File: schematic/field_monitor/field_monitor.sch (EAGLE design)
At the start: 4 parts, among them Q1 MOSFET-NCHANNELFQP30N06L

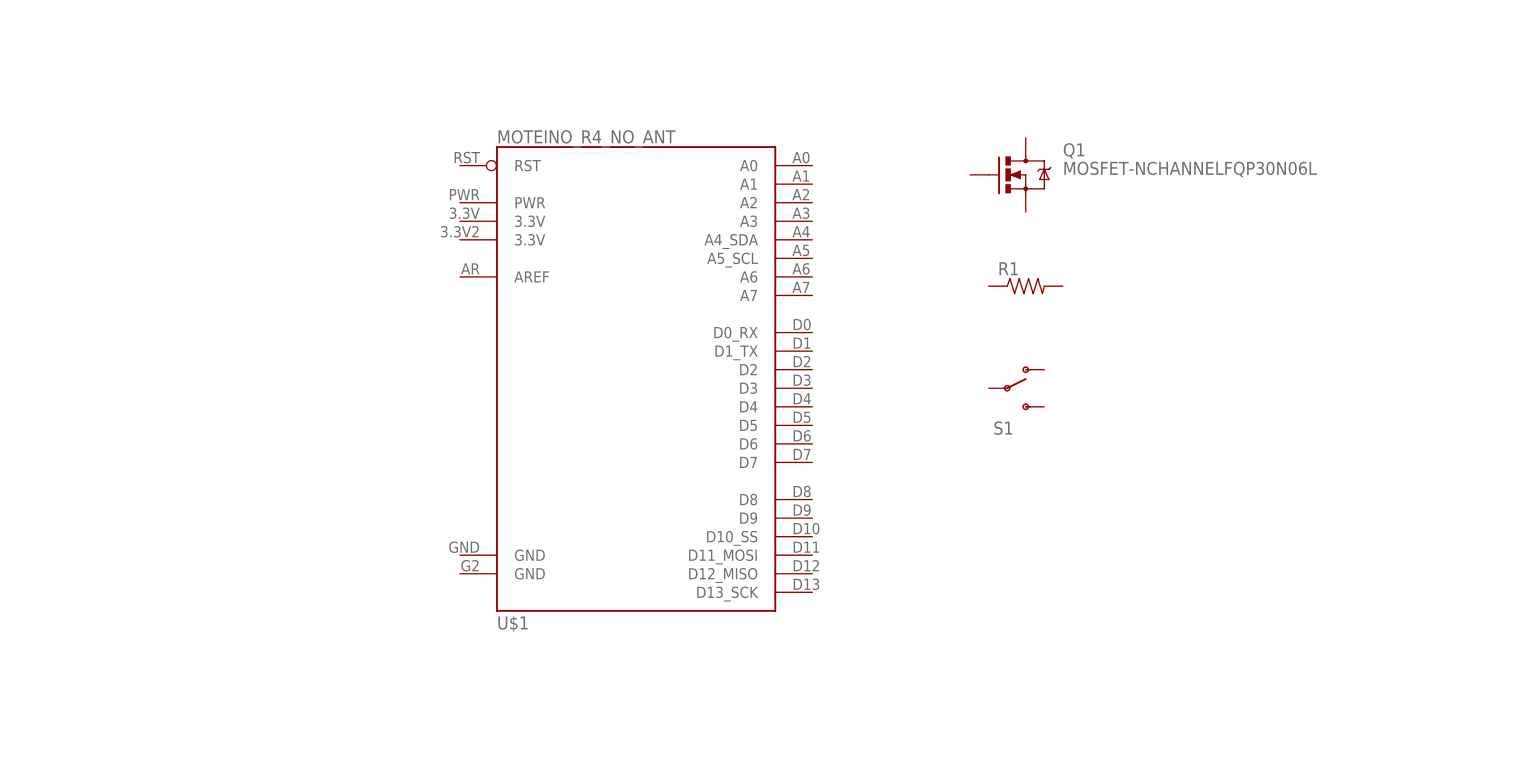
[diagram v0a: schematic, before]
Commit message: Adding basic components to schematic
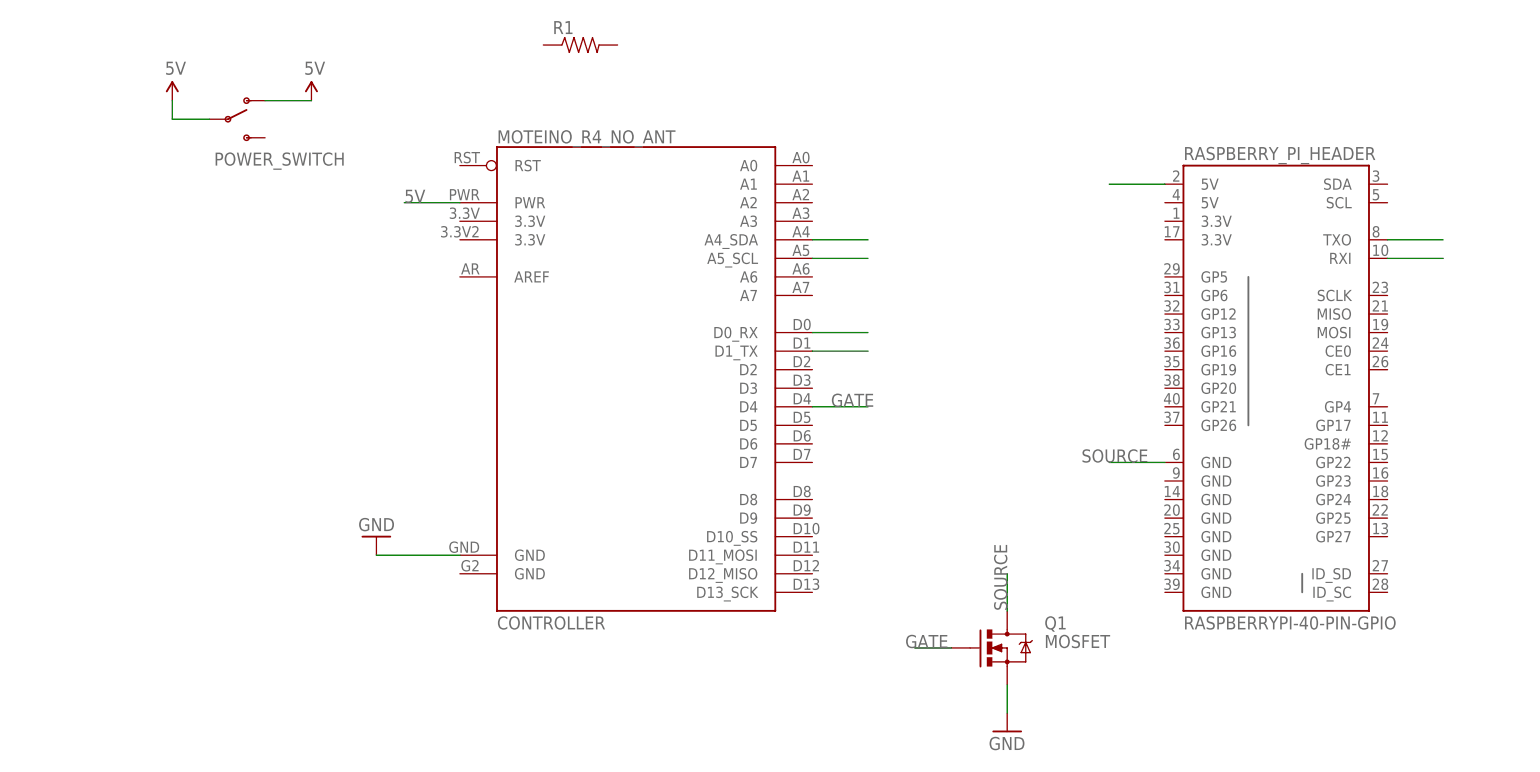
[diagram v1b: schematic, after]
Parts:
- removed S1: (no value), SparkFun-Electromechanical:SWITCH-SPDTPTH
- added POWER_SWITCH: (no value), SparkFun-Electromechanical:SWITCH-SPDTPTH
- added RASPBERRY_PI_HEADER: RASPBERRYPI-40-PIN-GPIO, SparkFun-Boards:RASPBERRYPI-40-PIN-GPIO
- Q1: value MOSFET-NCHANNELFQP30N06L -> MOSFET
- renumbered U$1 to CONTROLLER
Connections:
- new net 5V: CONTROLLER.PWR, POWER_SWITCH.O, POWER_SWITCH.P, RASPBERRY_PI_HEADER.5V@2
- new net GATE: CONTROLLER.D4, Q1.G
- new net GND: CONTROLLER.GND@1, Q1.S
- new net N$10: RASPBERRY_PI_HEADER.TXO
- new net N$11: RASPBERRY_PI_HEADER.RXI
- new net N$3: CONTROLLER.A5_SCL
- new net N$4: CONTROLLER.A4_SDA
- new net N$5: CONTROLLER.D0_RX
- new net N$6: CONTROLLER.D1_TX
- new net SOURCE: Q1.D, RASPBERRY_PI_HEADER.GND@6
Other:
- moved on the sheet: Q1, R1
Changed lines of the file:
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@@
 <layer number="112" name="tSilk" color="7" fill="1" visible="yes" active="yes"/>
 <layer number="113" name="IDFDebug" color="7" fill="1" visible="yes" active="yes"/>
+<layer number="114" name="Badge_Outline" color="11" fill="1" visible="no" active="no"/>
 <layer number="116" name="Patch_BOT" color="7" fill="1" visible="yes" active="yes"/>
 <layer number="118" name="Rect_Pads" color="7" fill="1" visible="yes" active="yes"/>
@@
 </classes>
 <parts>
-<part name="U$1" library="MoteinoR4Mod" deviceset="MOTEINO_R4_NO_ANT" device=""/>
-<part name="Q1" library="SparkFun-DiscreteSemi" deviceset="MOSFET-NCHANNEL" device="FQP30N06L"/>
+<part name="CONTROLLER" library="MoteinoR4Mod" deviceset="MOTEINO_R4_NO_ANT" device=""/>
+<part name="Q1" library="SparkFun-DiscreteSemi" deviceset="MOSFET-NCHANNEL" device="FQP30N06L" value="MOSFET"/>
 <part name="R1" library="SparkFun-Passives" deviceset="RESISTOR" device="PTH-1/4W"/>
-<part name="S1" library="SparkFun-Electromechanical" deviceset="SWITCH-SPDT" device="PTH"/>
+<part name="POWER_SWITCH" library="SparkFun-Electromechanical" deviceset="SWITCH-SPDT" device="PTH"/>
+<part name="RASPBERRY_PI_HEADER" library="SparkFun-Boards" deviceset="RASPBERRYPI-40-PIN-GPIO" device=""/>
+<part name="SUPPLY1" library="SparkFun-Aesthetics" deviceset="5V" device=""/>
+<part name="GND1" library="SparkFun-Aesthetics" deviceset="GND" device=""/>
+<part name="SUPPLY2" library="SparkFun-Aesthetics" deviceset="5V" device=""/>
+<part name="GND2" library="SparkFun-Aesthetics" deviceset="GND" device=""/>
 </parts>
 <sheets>
@@
 </plain>
 <instances>
-<instance part="U$1" gate="G$1" x="71.12" y="48.26"/>
-<instance part="Q1" gate="G$1" x="123.19" y="72.39"/>
-<instance part="R1" gate="G$1" x="123.19" y="57.15"/>
-<instance part="S1" gate="1" x="120.65" y="43.18"/>
+<instance part="CONTROLLER" gate="G$1" x="71.12" y="48.26"/>
+<instance part="Q1" gate="G$1" x="120.65" y="7.62"/>
+<instance part="R1" gate="G$1" x="62.23" y="90.17"/>
+<instance part="POWER_SWITCH" gate="1" x="13.97" y="80.01"/>
+<instance part="RASPBERRY_PI_HEADER" gate="G$1" x="157.48" y="45.72"/>
+<instance part="SUPPLY1" gate="G$1" x="6.35" y="82.55"/>
+<instance part="GND1" gate="1" x="34.29" y="22.86" rot="R180"/>
+<instance part="SUPPLY2" gate="G$1" x="25.4" y="82.55"/>
+<instance part="GND2" gate="1" x="120.65" y="-3.81"/>
 </instances>
 <busses>
 </busses>
 <nets>
+<net name="N$3" class="0">
+<segment>
+<pinref part="CONTROLLER" gate="G$1" pin="A5_SCL"/>
+<wire x1="93.98" y1="60.96" x2="101.6" y2="60.96" width="0.1524" layer="91"/>
+</segment>
+</net>
+<net name="N$4" class="0">
+<segment>
+<pinref part="CONTROLLER" gate="G$1" pin="A4_SDA"/>
+<wire x1="93.98" y1="63.5" x2="101.6" y2="63.5" width="0.1524" layer="91"/>
+</segment>
+</net>
+<net name="N$5" class="0">
+<segment>
+<pinref part="CONTROLLER" gate="G$1" pin="D0_RX"/>
+<wire x1="93.98" y1="50.8" x2="101.6" y2="50.8" width="0.1524" layer="91"/>
+</segment>
+</net>
+<net name="N$6" class="0">
+<segment>
+<pinref part="CONTROLLER" gate="G$1" pin="D1_TX"/>
+<wire x1="93.98" y1="48.26" x2="101.6" y2="48.26" width="0.1524" layer="91"/>
+</segment>
+</net>
+<net name="N$10" class="0">
+<segment>
+<pinref part="RASPBERRY_PI_HEADER" gate="G$1" pin="TXO"/>
+<wire x1="172.72" y1="63.5" x2="180.34" y2="63.5" width="0.1524" layer="91"/>
+</segment>
+</net>
+<net name="N$11" class="0">
+<segment>
+<pinref part="RASPBERRY_PI_HEADER" gate="G$1" pin="RXI"/>
+<wire x1="172.72" y1="60.96" x2="180.34" y2="60.96" width="0.1524" layer="91"/>
+</segment>
+</net>
+<net name="5V" class="0">
+<segment>
+<pinref part="SUPPLY1" gate="G$1" pin="5V"/>
+<wire x1="6.35" y1="82.55" x2="6.35" y2="80.01" width="0.1524" layer="91"/>
+<pinref part="POWER_SWITCH" gate="1" pin="P"/>
+<wire x1="6.35" y1="80.01" x2="11.43" y2="80.01" width="0.1524" layer="91"/>
+</segment>
+<segment>
+<pinref part="POWER_SWITCH" gate="1" pin="O"/>
+<pinref part="SUPPLY2" gate="G$1" pin="5V"/>
+<wire x1="19.05" y1="82.55" x2="25.4" y2="82.55" width="0.1524" layer="91"/>
+</segment>
+<segment>
+<pinref part="CONTROLLER" gate="G$1" pin="PWR"/>
+<wire x1="45.72" y1="68.58" x2="38.1" y2="68.58" width="0.1524" layer="91"/>
+<label x="38.1" y="68.58" size="1.778" layer="95"/>
+</segment>
+<segment>
+<pinref part="RASPBERRY_PI_HEADER" gate="G$1" pin="5V@2"/>
+<wire x1="142.24" y1="71.12" x2="134.62" y2="71.12" width="0.1524" layer="91"/>
+</segment>
+</net>
+<net name="GND" class="0">
+<segment>
+<pinref part="CONTROLLER" gate="G$1" pin="GND@1"/>
+<wire x1="45.72" y1="20.32" x2="34.29" y2="20.32" width="0.1524" layer="91"/>
+<pinref part="GND1" gate="1" pin="GND"/>
+</segment>
+<segment>
+<pinref part="Q1" gate="G$1" pin="S"/>
+<wire x1="120.65" y1="2.54" x2="120.65" y2="-1.27" width="0.1524" layer="91"/>
+<pinref part="GND2" gate="1" pin="GND"/>
+</segment>
+</net>
+<net name="GATE" class="0">
+<segment>
+<pinref part="Q1" gate="G$1" pin="G"/>
+<wire x1="113.03" y1="7.62" x2="107.95" y2="7.62" width="0.1524" layer="91"/>
+<label x="106.68" y="7.62" size="1.778" layer="95"/>
+</segment>
+<segment>
+<pinref part="CONTROLLER" gate="G$1" pin="D4"/>
+<wire x1="93.98" y1="40.64" x2="101.6" y2="40.64" width="0.1524" layer="91"/>
+<label x="96.52" y="40.64" size="1.778" layer="95"/>
+</segment>
+</net>
+<net name="SOURCE" class="0">
+<segment>
+<pinref part="RASPBERRY_PI_HEADER" gate="G$1" pin="GND@6"/>
+<wire x1="142.24" y1="33.02" x2="134.62" y2="33.02" width="0.1524" layer="91"/>
+<label x="130.81" y="33.02" size="1.778" layer="95"/>
+</segment>
+<segment>
+<pinref part="Q1" gate="G$1" pin="D"/>
+<wire x1="120.65" y1="12.7" x2="120.65" y2="17.78" width="0.1524" layer="91"/>
+<label x="120.65" y="12.7" size="1.778" layer="95" rot="R90"/>
+</segment>
+</net>
 </nets>
 </sheet>
